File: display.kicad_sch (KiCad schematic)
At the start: 13 parts, among them Q3 BSS138, U8 RS2299XTQC16

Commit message: ci: prepare files for CI
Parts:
- U8: footprint Package_DFN_QFN:QFN-16-1EP_3x3mm_P0.5mm_EP1.7x1.7mm -> Gigahawk:QFN-16-1EP_3x3mm_P0.5mm_EP1.7x1.7mm
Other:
- title: (none) -> piPod IO/SMC Board
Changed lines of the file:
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@@
 (kicad_sch (version 20211123) (generator eeschema)
   (paper "A4")
+  (title_block
+    (title "piPod IO/SMC Board")
+    (date "${DATE}")
+    (rev "%{TAG} (${REVISION})")
+  )
   (junction (at 232.41 109.22) (diameter 0) (color 0 0 0 0)
   )
@@
       (effects (font (size 1.27 1.27)) (justify right))
     )
-    (property "Footprint" "Package_DFN_QFN:QFN-16-1EP_3x3mm_P0.5mm_EP1.7x1.7mm" (id 2) (at 97.79 88.9 0)
-      (effects (font (size 1.27 1.27)) (justify left) hide)
-    )
+    (property "Footprint" "Gigahawk:QFN-16-1EP_3x3mm_P0.5mm_EP1.7x1.7mm" (id 2) (at 97.79 88.9 0)
+      (effects (font (size 1.27 1.27)) (justify left) hide)
+    )

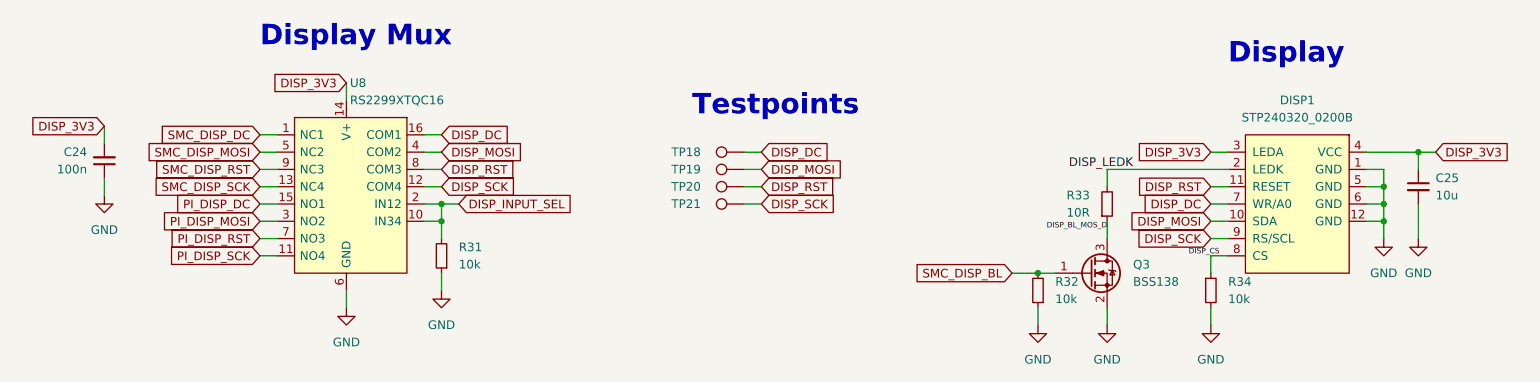
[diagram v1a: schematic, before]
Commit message: ci: test marking parts in sch for bom
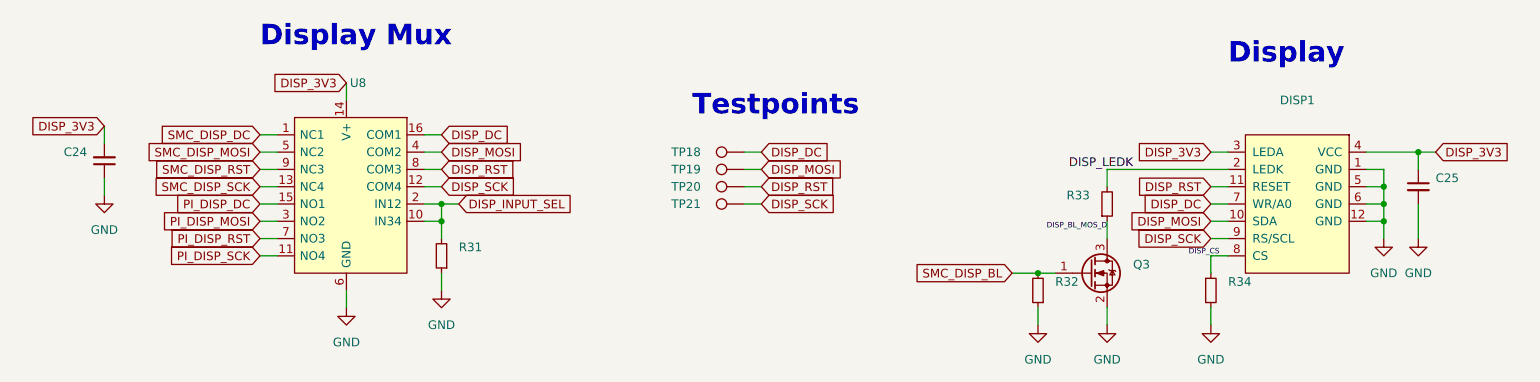
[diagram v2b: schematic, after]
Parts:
- C24: value 100n -> (none); footprint Capacitor_SMD:C_0402_1005Metric -> (none)
- C25: value 10u -> (none); footprint Capacitor_SMD:C_0402_1005Metric -> (none)
- DISP1: value STP240320_0200B -> (none); footprint Connector_Molex:Molex_SlimStack_54722-0164_2x08_P0.50mm_Vertical -> (none)
- Q3: value BSS138 -> (none); footprint Package_TO_SOT_SMD:SOT-23 -> (none)
- R31, R32, R34: value 10k -> (none); footprint Resistor_SMD:R_0402_1005Metric -> (none)
- R33: value 10R -> (none); footprint Resistor_SMD:R_0402_1005Metric -> (none)
- TP18, TP19, TP20, TP21: value TestPoint -> (none); footprint TestPoint:TestPoint_Pad_D1.5mm -> (none)
- U8: value RS2299XTQC16 -> (none); footprint Gigahawk:QFN-16-1EP_3x3mm_P0.5mm_EP1.7x1.7mm -> (none)
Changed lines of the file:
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@@
       (effects (font (size 1.27 1.27)) (justify right))
     )
-    (property "Value" "RS2299XTQC16" (id 1) (at 80.5306 96.52 0)
-      (effects (font (size 1.27 1.27)) (justify right))
-    )
-    (property "Footprint" "Gigahawk:QFN-16-1EP_3x3mm_P0.5mm_EP1.7x1.7mm" (id 2) (at 97.79 88.9 0)
+    (property "Value" "" (id 1) (at 80.5306 96.52 0)
+      (effects (font (size 1.27 1.27)) (justify right))
+    )
+    (property "Footprint" "" (id 2) (at 97.79 88.9 0)
       (effects (font (size 1.27 1.27)) (justify left) hide)
     )
@@
       (effects (font (size 1.27 1.27)) (justify left))
     )
-    (property "Value" "TestPoint" (id 1) (at 136.3979 104.14 0)
-      (effects (font (size 1.27 1.27)) (justify left) hide)
-    )
-    (property "Footprint" "TestPoint:TestPoint_Pad_D1.5mm" (id 2) (at 138.43 101.6 0)
+    (property "Value" "" (id 1) (at 136.3979 104.14 0)
+      (effects (font (size 1.27 1.27)) (justify left) hide)
+    )
+    (property "Footprint" "" (id 2) (at 138.43 101.6 0)
       (effects (font (size 1.27 1.27)) hide)
     )
@@
       (effects (font (size 1.27 1.27)) (justify right))
     )
-    (property "Value" "10R" (id 1) (at 189.23 113.0299 0)
-      (effects (font (size 1.27 1.27)) (justify right))
-    )
-    (property "Footprint" "Resistor_SMD:R_0402_1005Metric" (id 2) (at 191.77 111.76 0)
+    (property "Value" "" (id 1) (at 189.23 113.0299 0)
+      (effects (font (size 1.27 1.27)) (justify right))
+    )
+    (property "Footprint" "" (id 2) (at 191.77 111.76 0)
       (effects (font (size 1.27 1.27)) hide)
     )
@@
       (effects (font (size 1.27 1.27)) (justify left))
     )
-    (property "Value" "TestPoint" (id 1) (at 136.3979 101.6 0)
-      (effects (font (size 1.27 1.27)) (justify left) hide)
-    )
-    (property "Footprint" "TestPoint:TestPoint_Pad_D1.5mm" (id 2) (at 138.43 99.06 0)
+    (property "Value" "" (id 1) (at 136.3979 101.6 0)
+      (effects (font (size 1.27 1.27)) (justify left) hide)
+    )
+    (property "Footprint" "" (id 2) (at 138.43 99.06 0)
       (effects (font (size 1.27 1.27)) hide)
     )
@@
       (effects (font (size 1.27 1.27)) (justify left))
     )
-    (property "Value" "TestPoint" (id 1) (at 136.3979 106.68 0)
-      (effects (font (size 1.27 1.27)) (justify left) hide)
-    )
-    (property "Footprint" "TestPoint:TestPoint_Pad_D1.5mm" (id 2) (at 138.43 104.14 0)
+    (property "Value" "" (id 1) (at 136.3979 106.68 0)
+      (effects (font (size 1.27 1.27)) (justify left) hide)
+    )
+    (property "Footprint" "" (id 2) (at 138.43 104.14 0)
       (effects (font (size 1.27 1.27)) hide)
     )
@@
       (effects (font (size 1.27 1.27)) (justify right))
     )
-    (property "Value" "10k" (id 1) (at 96.52 120.6499 0)
-      (effects (font (size 1.27 1.27)) (justify right))
-    )
-    (property "Footprint" "Resistor_SMD:R_0402_1005Metric" (id 2) (at 93.98 119.38 0)
+    (property "Value" "" (id 1) (at 96.52 120.6499 0)
+      (effects (font (size 1.27 1.27)) (justify right))
+    )
+    (property "Footprint" "" (id 2) (at 93.98 119.38 0)
       (effects (font (size 1.27 1.27)) hide)
     )
@@
     (in_bom yes) (on_board yes) (fields_autoplaced)
     (property "Reference" "DISP1" (id 0) (at 219.71 96.52 0))
-    (property "Value" "STP240320_0200B" (id 1) (at 219.71 99.06 0))
-    (property "Footprint" "Connector_Molex:Molex_SlimStack_54722-0164_2x08_P0.50mm_Vertical" (id 2) (at 219.71 101.6 0)
+    (property "Value" "" (id 1) (at 219.71 99.06 0))
+    (property "Footprint" "" (id 2) (at 219.71 101.6 0)
       (effects (font (size 1.27 1.27)) hide)
     )
@@
       (effects (font (size 1.27 1.27)) (justify right))
     )
-    (property "Value" "10k" (id 1) (at 184.15 125.7299 0)
-      (effects (font (size 1.27 1.27)) (justify right))
-    )
-    (property "Footprint" "Resistor_SMD:R_0402_1005Metric" (id 2) (at 181.61 124.46 0)
+    (property "Value" "" (id 1) (at 184.15 125.7299 0)
+      (effects (font (size 1.27 1.27)) (justify right))
+    )
+    (property "Footprint" "" (id 2) (at 181.61 124.46 0)
       (effects (font (size 1.27 1.27)) hide)
     )
@@
       (effects (font (size 1.27 1.27)) (justify left))
     )
-    (property "Value" "10k" (id 1) (at 209.55 125.7299 0)
-      (effects (font (size 1.27 1.27)) (justify left))
-    )
-    (property "Footprint" "Resistor_SMD:R_0402_1005Metric" (id 2) (at 207.01 124.46 0)
+    (property "Value" "" (id 1) (at 209.55 125.7299 0)
+      (effects (font (size 1.27 1.27)) (justify left))
+    )
+    (property "Footprint" "" (id 2) (at 207.01 124.46 0)
       (effects (font (size 1.27 1.27)) hide)
     )
@@
       (effects (font (size 1.27 1.27)) (justify left))
     )
-    (property "Value" "10u" (id 1) (at 240.03 110.4962 0)
-      (effects (font (size 1.27 1.27)) (justify left))
-    )
-    (property "Footprint" "Capacitor_SMD:C_0402_1005Metric" (id 2) (at 237.49 109.22 0)
+    (property "Value" "" (id 1) (at 240.03 110.4962 0)
+      (effects (font (size 1.27 1.27)) (justify left))
+    )
+    (property "Footprint" "" (id 2) (at 237.49 109.22 0)
       (effects (font (size 1.27 1.27)) hide)
     )
@@
       (effects (font (size 1.27 1.27)) (justify right))
     )
-    (property "Value" "100n" (id 1) (at 41.91 106.6735 0)
-      (effects (font (size 1.27 1.27)) (justify right))
-    )
-    (property "Footprint" "Capacitor_SMD:C_0402_1005Metric" (id 2) (at 44.45 105.41 0)
+    (property "Value" "" (id 1) (at 41.91 106.6735 0)
+      (effects (font (size 1.27 1.27)) (justify right))
+    )
+    (property "Footprint" "" (id 2) (at 44.45 105.41 0)
       (effects (font (size 1.27 1.27)) hide)
     )
@@
       (effects (font (size 1.27 1.27)) (justify left))
     )
-    (property "Value" "BSS138" (id 1) (at 195.58 123.1899 0)
-      (effects (font (size 1.27 1.27)) (justify left))
-    )
-    (property "Footprint" "Package_TO_SOT_SMD:SOT-23" (id 2) (at 194.31 123.825 0)
+    (property "Value" "" (id 1) (at 195.58 123.1899 0)
+      (effects (font (size 1.27 1.27)) (justify left))
+    )
+    (property "Footprint" "" (id 2) (at 194.31 123.825 0)
       (effects (font (size 1.27 1.27) italic) (justify left) hide)
     )
@@
       (effects (font (size 1.27 1.27)) (justify left))
     )
-    (property "Value" "TestPoint" (id 1) (at 136.3979 109.22 0)
-      (effects (font (size 1.27 1.27)) (justify left) hide)
-    )
-    (property "Footprint" "TestPoint:TestPoint_Pad_D1.5mm" (id 2) (at 138.43 106.68 0)
-      (effects (font (size 1.27 1.27)) hide)
-    )
+    (property "Value" "" (id 1) (at 136.3979 109.22 0)
+      (effects (font (size 1.27 1.27)) (justify left) hide)
+    )
+    (property "Footprint" "" (id 2) (at 138.43 106.68 0)
+      (effects (font (size 1.27 1.27)) hide)
+    )
